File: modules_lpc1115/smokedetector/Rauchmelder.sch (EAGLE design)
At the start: 75 parts, among them IC1 BD9G101, IC2 LPC1115, Q1 BC856, Q3 BCP52, Q4 ASFL, T1 BC847C, T2 BC817

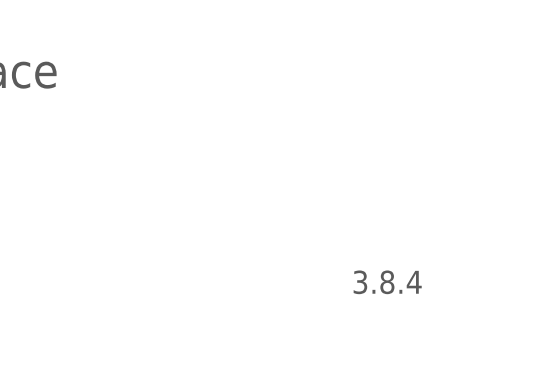
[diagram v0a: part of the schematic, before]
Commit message: [RM] -  smaller positioning changes; increased version
set version from 3.8.x to 3.9.x because of switch to 0805 which is a quite big change
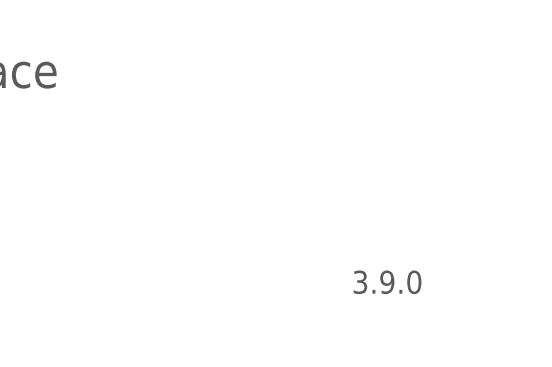
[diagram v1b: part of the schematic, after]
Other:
- note added: "3.9.0"
- note removed: "3.8.4"
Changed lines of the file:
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@@
 <text x="317.5" y="27.94" size="2.54" layer="97">www.selfbus.org</text>
 <text x="320.04" y="10.16" size="2.54" layer="97">Rauchmelder ARM</text>
-<text x="403.86" y="10.16" size="2.54" layer="97">3.8.4</text>
+<text x="403.86" y="10.16" size="2.54" layer="97">3.9.0</text>
 <text x="193.04" y="165.1" size="1.778" layer="91">6 to RXD and P00</text>
 <text x="193.04" y="162.56" size="1.778" layer="91">7 to TXD and P01</text>

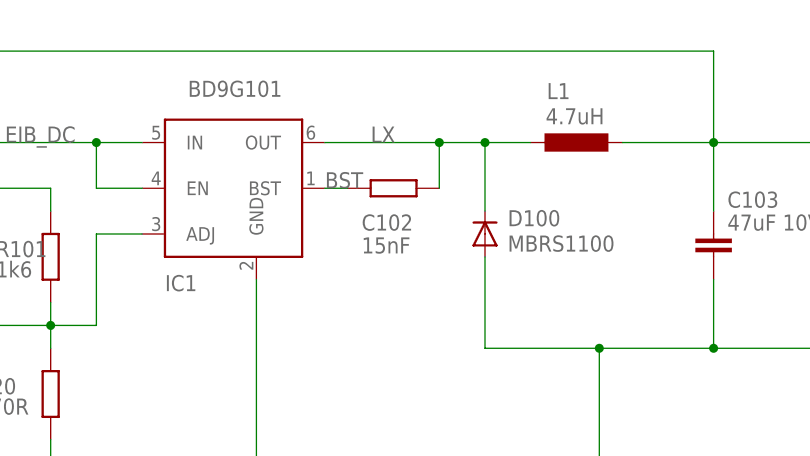
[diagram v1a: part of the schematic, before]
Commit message: [RM] - corrected wrong part for C102 and error in solder topcoat
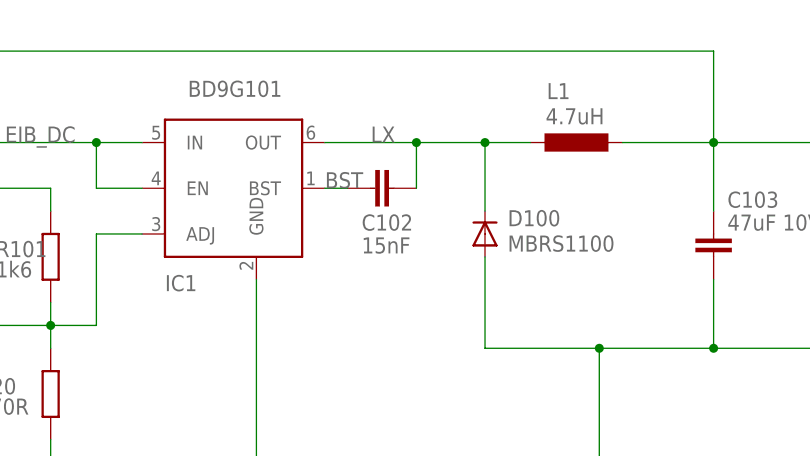
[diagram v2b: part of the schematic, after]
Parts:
- C102: device rcl:R-EU_R0805 -> rcl:C-EUC0805
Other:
- moved on the sheet: C102
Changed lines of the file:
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@@
 <part name="C100" library="rcl" library_urn="urn:adsk.eagle:library:334" deviceset="C-EU" device="C0805" package3d_urn="urn:adsk.eagle:package:23617/2" value="4.7uF 50V"/>
 <part name="C103" library="rcl" library_urn="urn:adsk.eagle:library:334" deviceset="C-EU" device="C0805" package3d_urn="urn:adsk.eagle:package:23617/2" value="47uF 10V"/>
-<part name="C102" library="rcl" library_urn="urn:adsk.eagle:library:334" deviceset="R-EU_" device="R0805" package3d_urn="urn:adsk.eagle:package:23553/2" value="15nF"/>
+<part name="C102" library="rcl" library_urn="urn:adsk.eagle:library:334" deviceset="C-EU" device="C0805" package3d_urn="urn:adsk.eagle:package:23617/2" value="15nF"/>
 <part name="R101" library="rcl" library_urn="urn:adsk.eagle:library:334" deviceset="R-EU_" device="R0805" package3d_urn="urn:adsk.eagle:package:23553/2" value="1k6"/>
 <part name="R20" library="rcl" library_urn="urn:adsk.eagle:library:334" deviceset="R-EU_" device="R0805" package3d_urn="urn:adsk.eagle:package:23553/2" value="470R"/>
@@
 <attribute name="VALUE" x="136.144" y="215.519" size="1.778" layer="96" rot="MR180"/>
 </instance>
-<instance part="C102" gate="G$1" x="99.06" y="218.44" smashed="yes" rot="R180">
+<instance part="C102" gate="G$1" x="99.06" y="218.44" smashed="yes" rot="R270">
 <attribute name="NAME" x="95.504" y="213.741" size="1.778" layer="95"/>
 <attribute name="VALUE" x="95.504" y="211.201" size="1.778" layer="96"/>
@@
 <segment>
 <pinref part="IC1" gate="G$1" pin="OUT"/>
-<wire x1="91.44" y1="223.52" x2="104.14" y2="223.52" width="0.1524" layer="91"/>
+<wire x1="91.44" y1="223.52" x2="101.6" y2="223.52" width="0.1524" layer="91"/>
 <pinref part="C102" gate="G$1" pin="1"/>
-<wire x1="104.14" y1="223.52" x2="109.22" y2="223.52" width="0.1524" layer="91"/>
+<wire x1="101.6" y1="223.52" x2="109.22" y2="223.52" width="0.1524" layer="91"/>
 <wire x1="109.22" y1="223.52" x2="114.3" y2="223.52" width="0.1524" layer="91"/>
-<wire x1="104.14" y1="218.44" x2="104.14" y2="223.52" width="0.1524" layer="91"/>
+<wire x1="101.6" y1="218.44" x2="101.6" y2="223.52" width="0.1524" layer="91"/>
 <pinref part="L1" gate="G$1" pin="1"/>
 <wire x1="109.22" y1="215.9" x2="109.22" y2="223.52" width="0.1524" layer="91"/>
-<junction x="104.14" y="223.52"/>
+<junction x="101.6" y="223.52"/>
 <junction x="109.22" y="223.52"/>
 <pinref part="D100" gate="G$1" pin="C"/>
